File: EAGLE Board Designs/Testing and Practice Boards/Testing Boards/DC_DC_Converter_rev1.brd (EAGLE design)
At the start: 104.4 x 55 mm, 9 parts

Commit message: fixed git's fun with dc-dc
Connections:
- net -BATTERY renamed IN-
- net N$1 renamed IN+
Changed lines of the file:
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@@
 </elements>
 <signals>
-<signal name="-BATTERY">
+<signal name="IN-">
 <contactref element="U$1" pad="2"/>
 <contactref element="U$3" pad="2"/>
@@
 <wire x1="10.6" y1="-50.59" x2="14.8" y2="-50.59" width="0" layer="19" extent="1-1"/>
 </signal>
-<signal name="N$1">
+<signal name="IN+">
 <contactref element="U$1" pad="1"/>
 <contactref element="U$2" pad="2"/>

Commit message: Finished dc dc board
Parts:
- moved C1 148.1 mm to (25.0, 41.9), turned to 180 degrees
- moved J1 131.1 mm to (97.5, 46.6), turned to 180 degrees
- moved F1 129.8 mm to (81.0, 46.6)
- moved J2 117.0 mm to (10.0, 50.8), turned to 90 degrees
- moved J3 110.6 mm to (10.0, 43.8), turned to 90 degrees
- moved U$3 110.0 mm to (33.9, 19.4), turned to 270 degrees
- moved C2 99.8 mm to (62.1, 44.7), turned to 90 degrees
- moved U$2 96.5 mm to (17.5, 19.3), turned to 270 degrees
- moved U$1 43.5 mm to (8.64, 19.9), flipped to the bottom, turned to 180 degrees
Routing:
- net IN-: track 0.00 -> 65.7 mm
- net IN+: track 0.00 -> 61.5 mm
- net HV-: track 0.00 -> 46.0 mm
- net HV+: track 0.00 -> 39.9 mm
- net 12V_UNFUSED: track 0.00 -> 18.6 mm
- net GND: track 0.00 -> 14.0 mm
- added copper zone on layer 1, net +12V
- removed copper zone on layer 1, net 12V_FUSED
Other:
- board size 104.4 x 55 mm -> 99.4 x 55 mm

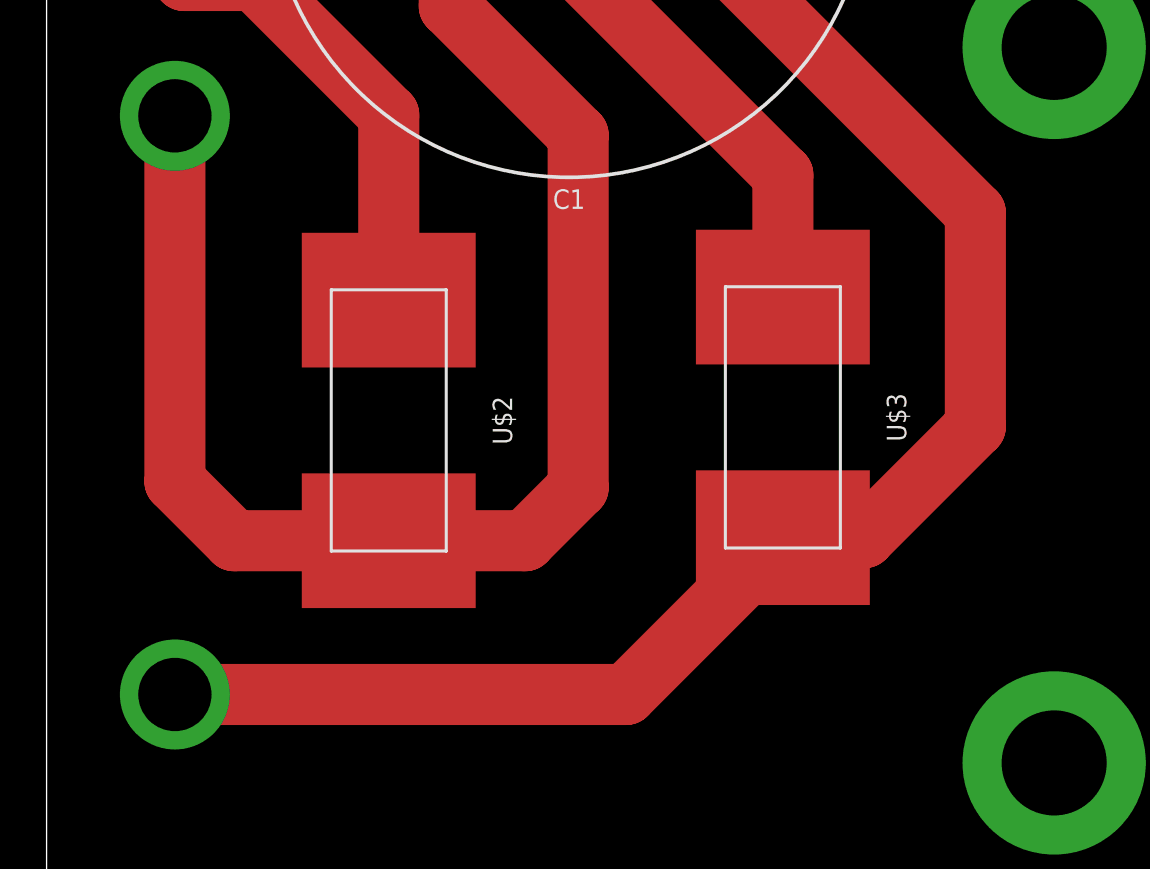
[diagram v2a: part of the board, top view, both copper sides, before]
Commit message: Updated dc dc converter
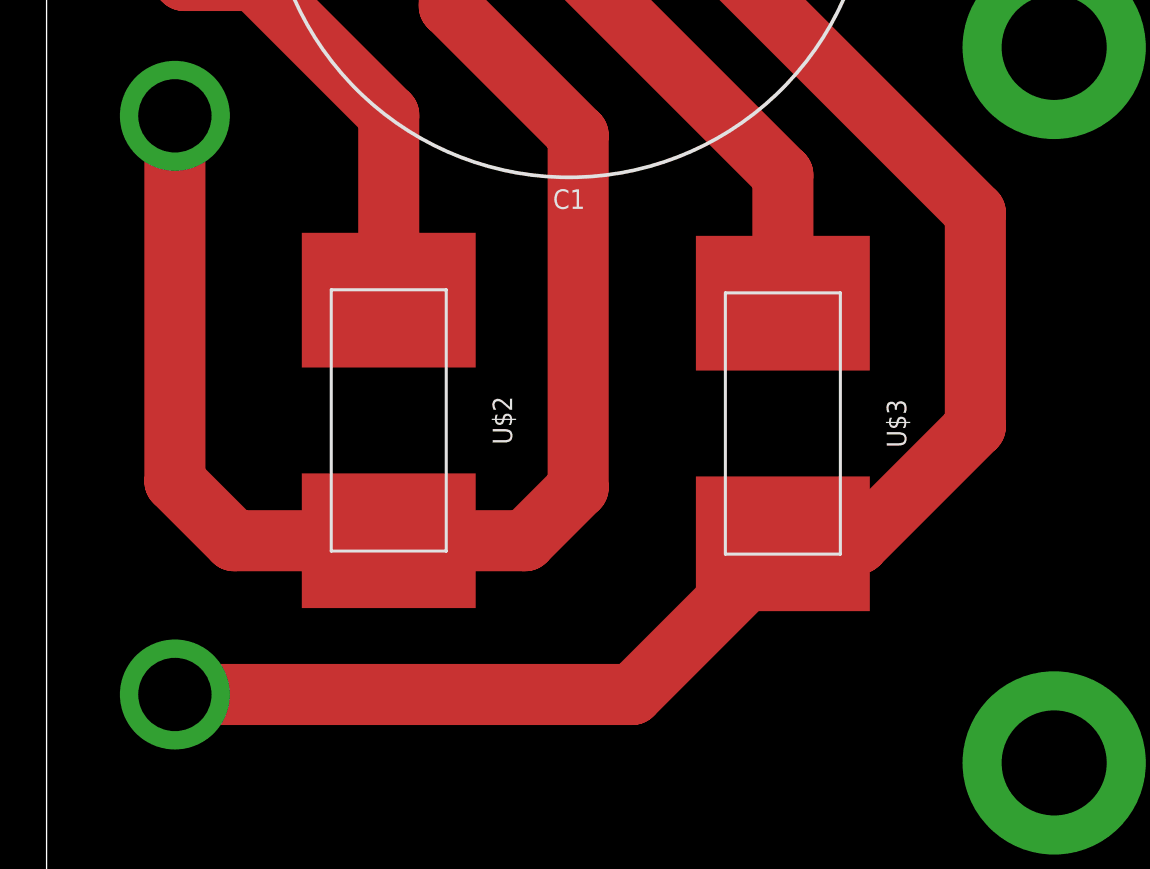
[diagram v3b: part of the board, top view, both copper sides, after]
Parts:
- moved U$3 0.25 mm to (33.9, 19.2)
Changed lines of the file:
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@@
 <attribute name="NAME" x="21.844" y="19.304" size="0.8128" layer="21" font="vector" rot="R270" align="bottom-center"/>
 </element>
-<element name="U$3" library="HyTechDevices" package="0885" value="885_FUSE" x="33.909" y="19.431" smashed="yes" rot="R270">
-<attribute name="NAME" x="38.227" y="19.431" size="0.8128" layer="21" font="vector" rot="R270" align="bottom-center"/>
+<element name="U$3" library="HyTechDevices" package="0885" value="885_FUSE" x="33.909" y="19.177" smashed="yes" rot="R270">
+<attribute name="NAME" x="38.227" y="19.177" size="0.8128" layer="21" font="vector" rot="R270" align="bottom-center"/>
 </element>
 <element name="C1" library="HyTechDevices" package="L*A" value="LGG2G181MELA25" x="25.019" y="41.91" smashed="yes" rot="R180">
@@
 <contactref element="U$3" pad="2"/>
 <contactref element="C1" pad="-"/>
-<wire x1="8.636" y1="7.9121" x2="27.3901" y2="7.9121" width="2.54" layer="1"/>
-<wire x1="27.3901" y1="7.9121" x2="33.909" y2="14.431" width="2.54" layer="1"/>
-<wire x1="33.909" y1="14.431" x2="37.291" y2="14.431" width="2.54" layer="1"/>
-<wire x1="37.291" y1="14.431" x2="41.91" y2="19.05" width="2.54" layer="1"/>
+<wire x1="8.636" y1="7.9121" x2="27.6441" y2="7.9121" width="2.54" layer="1"/>
+<wire x1="27.6441" y1="7.9121" x2="33.909" y2="14.177" width="2.54" layer="1"/>
+<wire x1="33.909" y1="14.177" x2="37.037" y2="14.177" width="2.54" layer="1"/>
+<wire x1="37.037" y1="14.177" x2="41.91" y2="19.05" width="2.54" layer="1"/>
 <wire x1="41.91" y1="19.05" x2="41.91" y2="27.94" width="2.54" layer="1"/>
 <wire x1="30.019" y1="39.831" x2="30.019" y2="41.91" width="2.54" layer="1"/>
@@
 <wire x1="10.033" y1="42.565" x2="10.688" y2="42.565" width="2.54" layer="1"/>
 <wire x1="10.688" y1="42.565" x2="11.938" y2="43.815" width="2.54" layer="1"/>
-<wire x1="33.909" y1="24.431" x2="33.909" y2="29.511" width="2.54" layer="1"/>
+<wire x1="33.909" y1="24.177" x2="33.909" y2="29.511" width="2.54" layer="1"/>
 <wire x1="33.909" y1="29.511" x2="25.4" y2="38.02" width="2.54" layer="1"/>
 <wire x1="25.4" y1="38.02" x2="25.4" y2="45.72" width="2.54" layer="1"/>

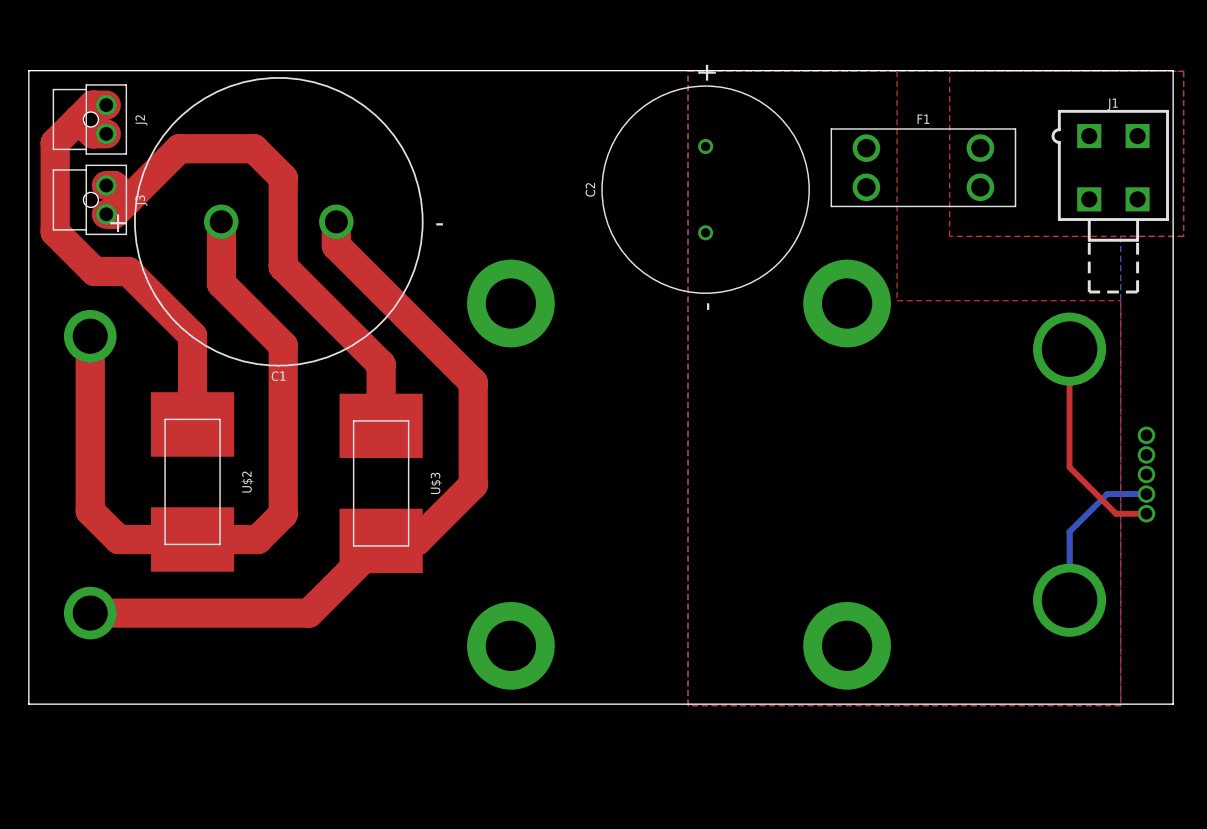
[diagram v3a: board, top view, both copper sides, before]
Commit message: Updated dc dc converter board design
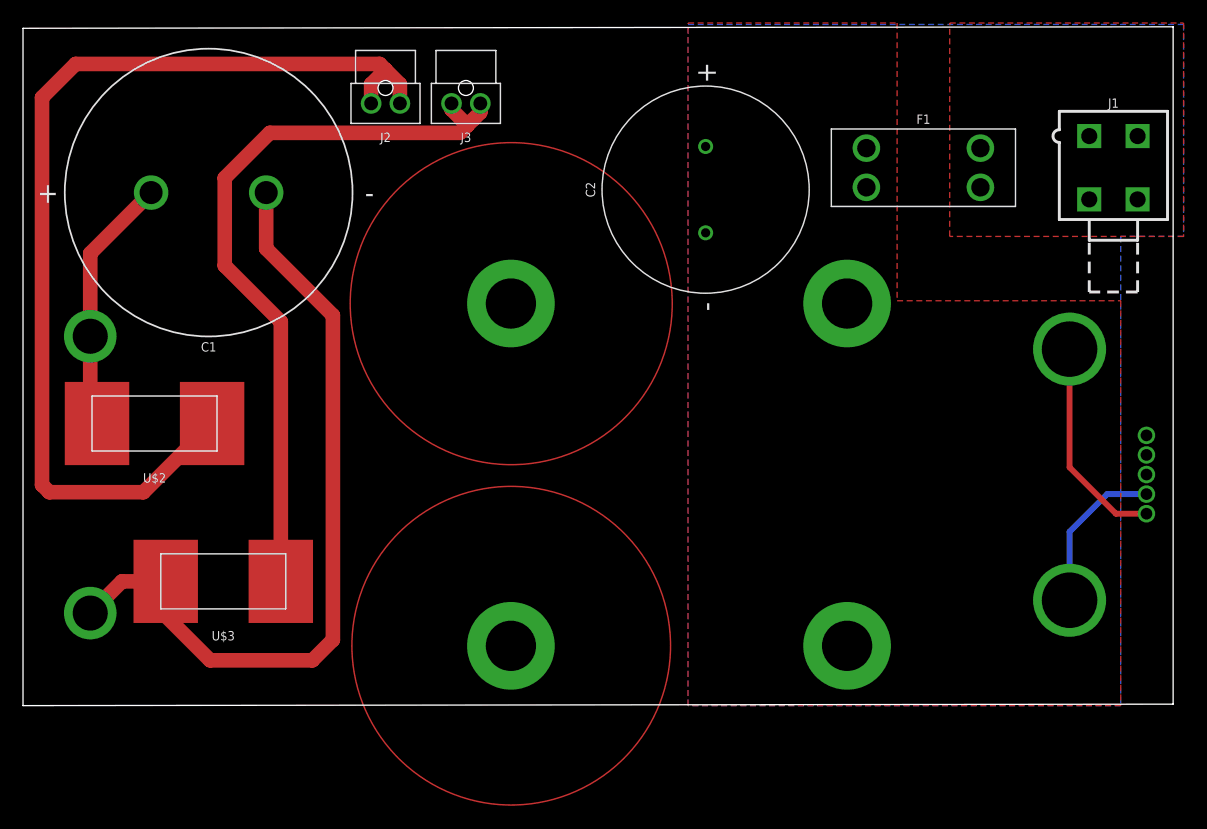
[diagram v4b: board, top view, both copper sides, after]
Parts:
- moved J3 32.3 mm to (41.3, 52.2), turned to 0 degrees
- moved J2 24.3 mm to (34.3, 52.2), turned to 0 degrees
- moved U$3 16.1 mm to (20.2, 10.7), turned to 180 degrees
- moved C1 6.60 mm to (18.9, 44.5)
- moved U$2 6.06 mm to (14.2, 24.4), turned to 180 degrees
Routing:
- net HV+: track 39.9 -> 89.3 mm
- net IN+: track 61.5 -> 23.6 mm
- net HV-: track 46.3 -> 64.9 mm
- net IN-: track 65.7 -> 68.8 mm
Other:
- board size 99.4 x 55 mm -> 99.9 x 59 mm

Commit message: Made final changes to DC DC Converter Board
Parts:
- C1: value LGG2G181MELA25 -> 4.7 mF; device HyTechDevices:L*A -> HyTechDevices:EKYC*MM
- C2: value (none) -> LGG2G181MELA25; device HyTechDevices:EKYC*MM -> HyTechDevices:L*A
- J1: device HyTechDevices:MOLEX_MINIFIT_PTH_04 -> HyTechDevices:MOLEX_NANOFIT_PTH_02
- J3: device HyTechDevices:MOLEX_NANOFIT_PTH_02 -> HyTechDevices:MOLEX_MINIFIT_PTH_04
- moved J1 64.0 mm to (33.8, 52.2), turned to 0 degrees
- moved J3 56.5 mm to (97.5, 46.6), turned to 180 degrees
- moved C1 43.2 mm to (62.1, 46.0), turned to 90 degrees
- moved C2 43.2 mm to (18.9, 44.5), turned to 180 degrees
- moved J2 6.22 mm to (40.5, 52.2)
- renumbered U$1 to U1, U$2 to F2, U$3 to F3
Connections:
- net +12V: now also J3.1, J3.2; no longer J1.1, J1.2
- net 12V_UNFUSED: now also C1.+; no longer C2.+
- net GND: now also C1.-, J3.3, J3.4; no longer C2.-, J1.3, J1.4
- net HV+: now also J1.1, J1.2; no longer J2.1, J2.2
- net HV-: now also J2.1, J2.2; no longer J3.1, J3.2
- net IN+: now also C2.+; no longer C1.+
- net IN-: now also C2.-; no longer C1.-
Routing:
- net HV-: track 64.9 -> 67.9 mm
- net HV+: track 89.3 -> 90.9 mm
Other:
- board size 99.9 x 59 mm -> 99.9 x 58.7 mm
- board text added: "Hytech Racing 2021 DC DC Converter Board Rev 1 By: Cody Kaminsky"
